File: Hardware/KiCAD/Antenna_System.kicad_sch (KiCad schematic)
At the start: 1 part, among them J2 Conn_Coaxial

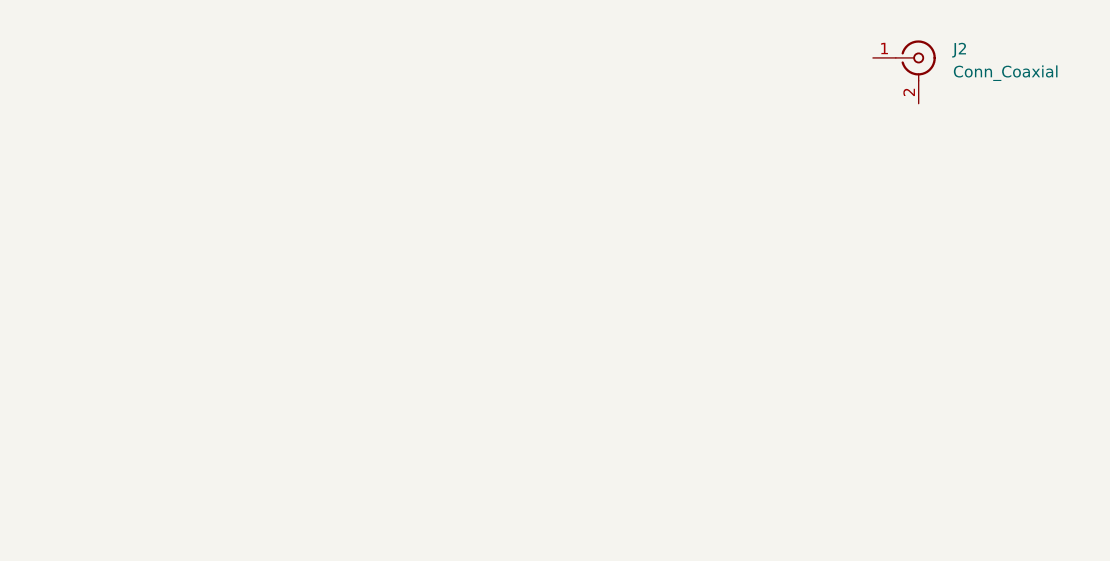
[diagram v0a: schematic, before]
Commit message: fix: Change some global labels to heirarchical
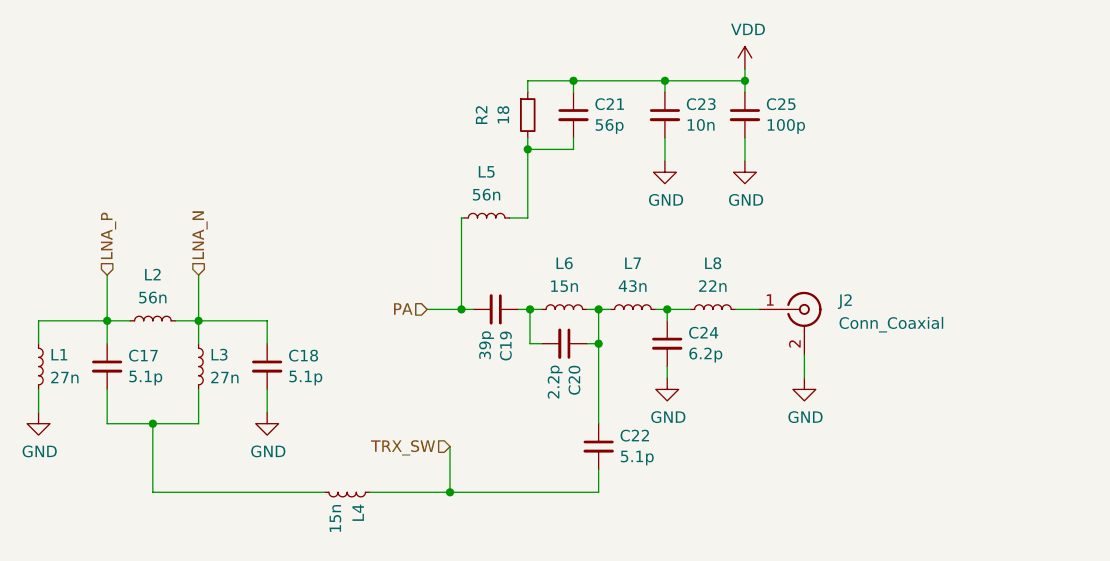
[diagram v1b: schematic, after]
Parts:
- added C17, C18, C22: 5.1p, Capacitor_SMD:C_0402_1005Metric, symbol pkl_device:pkl_C_Small
- added C19: 39p, Capacitor_SMD:C_0402_1005Metric, symbol pkl_device:pkl_C_Small
- added C20: 2.2p, Capacitor_SMD:C_0402_1005Metric, symbol pkl_device:pkl_C_Small
- added C21: 56p, Capacitor_SMD:C_0402_1005Metric, symbol pkl_device:pkl_C_Small
- added C23: 10n, Capacitor_SMD:C_0402_1005Metric, symbol pkl_device:pkl_C_Small
- added C24: 6.2p, Capacitor_SMD:C_0402_1005Metric, symbol pkl_device:pkl_C_Small
- added C25: 100p, Capacitor_SMD:C_0402_1005Metric, symbol pkl_device:pkl_C_Small
- added L1, L3: 27n, Inductor_SMD:L_0402_1005Metric, symbol Device:L_Small
- added L2, L5: 56n, Inductor_SMD:L_0402_1005Metric, symbol Device:L_Small
- added L4, L6: 15n, Inductor_SMD:L_0402_1005Metric, symbol Device:L_Small
- added L7: 43n, Inductor_SMD:L_0402_1005Metric, symbol Device:L_Small
- added L8: 22n, Inductor_SMD:L_0402_1005Metric, symbol Device:L_Small
- added R2: 18, Resistor_SMD:R_0402_1005Metric, symbol pkl_device:pkl_R_Small
- J2: footprint (none) -> Connector_Coaxial:SMA_Amphenol_901-143_Horizontal
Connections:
- net at J2.1 (In): now also L8.2
- net GND: now reaches J2.2 (Ext)
- net GND: now also C18.2, C23.2, C24.2, C25.2, L1.2
- new net: C20.1, C22.1, L6.2, L7.1
- new net: C24.1, L7.2, L8.1
- new net: C21.2, L5.2, R2.2
- new net: C19.1, C20.2, L6.1
- new net: C17.2, L3.2, L4.2
- new net LNA_N: C18.1, L2.2, L3.1
- new net LNA_P: C17.1, L1.1, L2.1
- new net PA: C19.2, L5.1
- new net TRX_SW: C22.2, L4.1
- new net VDD: C21.1, C23.1, C25.1, R2.1
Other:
- moved on the sheet: J2

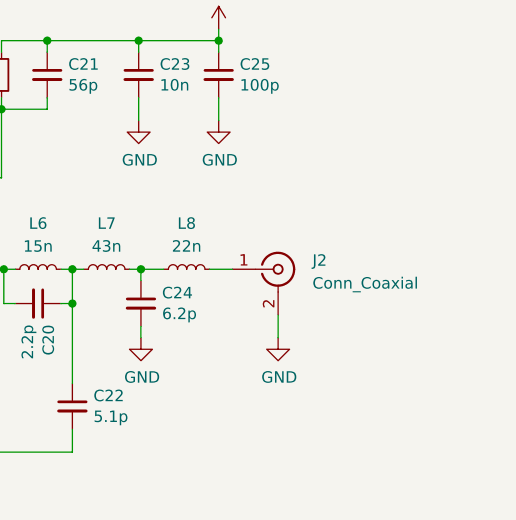
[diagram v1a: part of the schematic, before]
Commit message: Renamed and added the kicad library
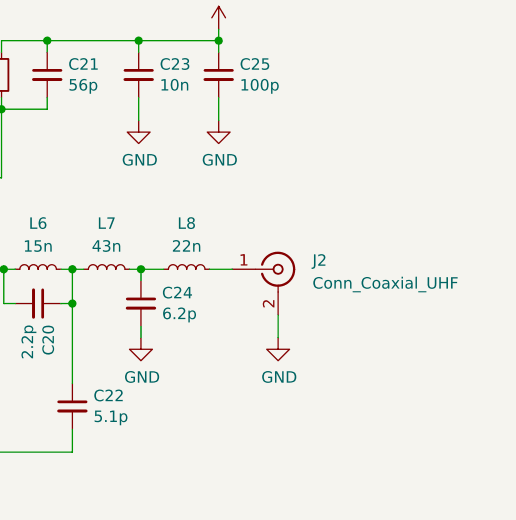
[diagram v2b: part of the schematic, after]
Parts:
- J2: value Conn_Coaxial -> Conn_Coaxial_UHF
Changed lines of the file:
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@@
       (effects (font (size 1.27 1.27)) (justify left))
     )
-    (property "Value" "Conn_Coaxial" (at 241.3 93.0032 0)
+    (property "Value" "Conn_Coaxial_UHF" (at 241.3 93.0032 0)
       (effects (font (size 1.27 1.27)) (justify left))
     )

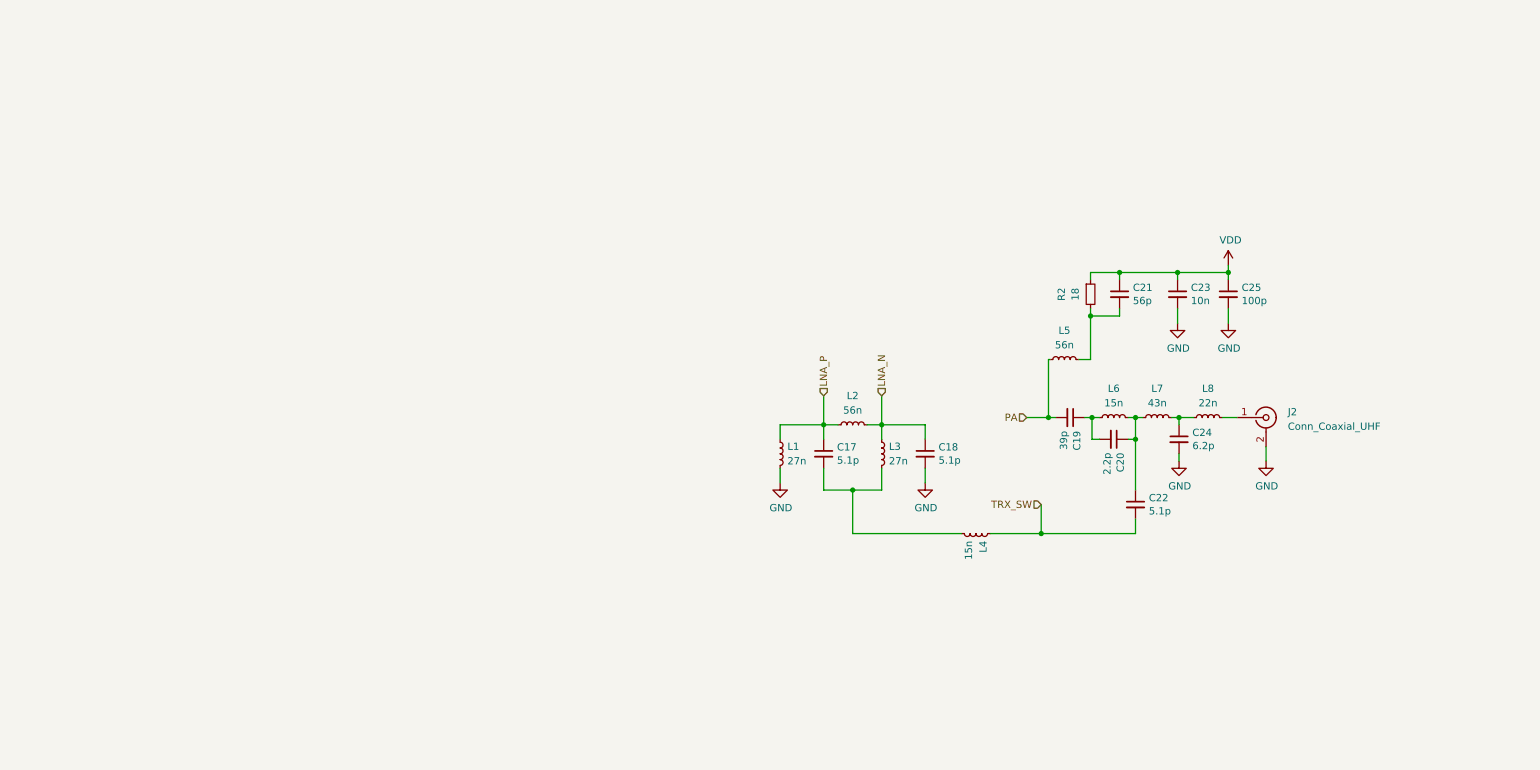
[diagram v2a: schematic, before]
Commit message: feat: corrected Power routing, added TODOs for board, prepared for amps
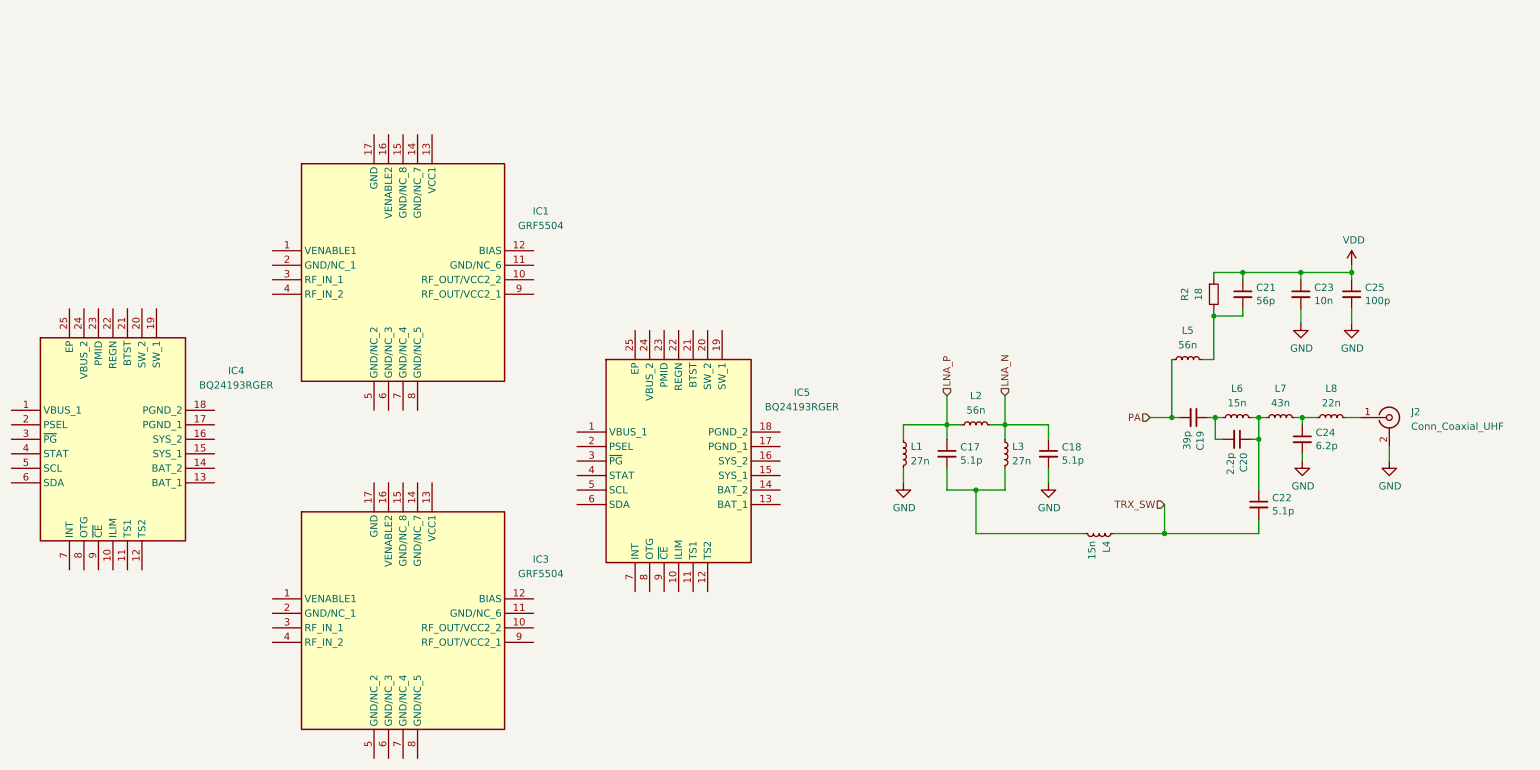
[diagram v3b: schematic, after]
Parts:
- added IC1, IC3: GRF5504, Cobalt_Cowboy:QFN50P300X300X90-17N_GRF5504, symbol Cobalt-Cowboy:GRF5504
- added IC4, IC5: BQ24193RGER, Cobalt_Cowboy:QFN50P400X400X100-25N-D_BQ24193RGER, symbol Cobalt-Cowboy:BQ24193RGER
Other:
- moved on the sheet: C17, C18, C19, C20, C21, C22, C23, C24, C25, J2, L1, L2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
